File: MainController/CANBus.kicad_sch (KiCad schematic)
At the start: 1 part, among them J2 Conn_01x04_Pin

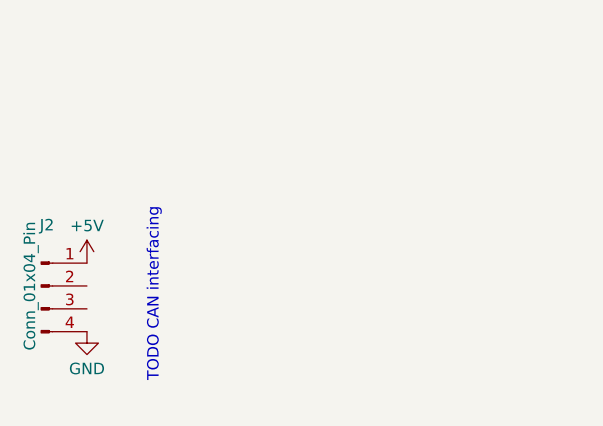
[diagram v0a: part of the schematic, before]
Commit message: WIP - Starting Voltage Measurement
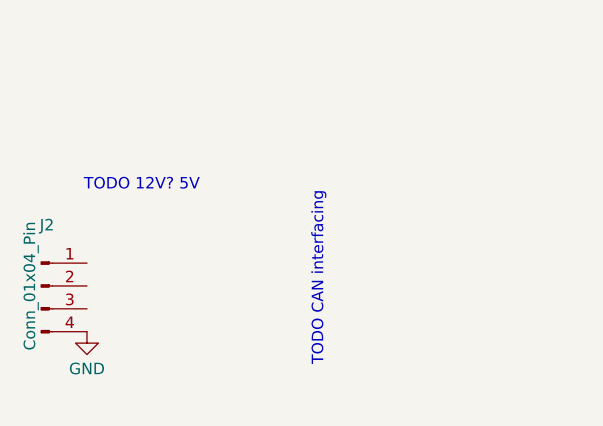
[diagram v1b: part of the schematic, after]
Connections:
- net +5V: no longer names the net of J2.1 (Pin_1)
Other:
- note added: "TODO 12V? 5V"
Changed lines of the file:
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@@
 	(text "TODO CAN interfacing"
 		(exclude_from_sim no)
-		(at 79.756 101.346 90)
+		(at 98.044 99.568 90)
+		(effects
+			(font
+				(size 1.27 1.27)
+			)
+		)
+	)
+	(text "TODO 12V? 5V"
+		(exclude_from_sim no)
+		(at 78.486 89.154 0)
 		(effects
 			(font
@@
 	(label "CAN_L"
 		(at 275.59 19.05 180)
-		(fields_autoplaced yes)
 		(effects
 			(font
@@
 	(label "CAN_H"
 		(at 275.59 15.24 180)
-		(fields_autoplaced yes)
 		(effects
 			(font
@@
 		(shape input)
 		(at 275.59 15.24 0)
-		(fields_autoplaced yes)
 		(effects
 			(font
@@
 		(shape input)
 		(at 275.59 19.05 0)
-		(fields_autoplaced yes)
 		(effects
 			(font
@@
 					(unit 1)
 				)
-			)
-		)
-	)
-	(symbol
-		(lib_id "power:+5V")
-		(at 72.39 97.79 0)
-		(unit 1)
-		(exclude_from_sim no)
-		(in_bom yes)
-		(on_board yes)
-		(dnp no)
-		(fields_autoplaced yes)
-		(property "Reference" "#PWR04"
-			(at 72.39 101.6 0)
-			(effects
-				(font
-					(size 1.27 1.27)
-				)
-				(hide yes)
-			)
-		)
-		(property "Value" "+5V"
-			(at 72.39 93.6569 0)
-			(effects
-				(font
-					(size 1.27 1.27)
-				)
-			)
-		)
-		(property "Footprint" ""
-			(at 72.39 97.79 0)
-			(effects
-				(font
-					(size 1.27 1.27)
-				)
-				(hide yes)
-			)
-		)
-		(property "Datasheet" ""
-			(at 72.39 97.79 0)
-			(effects
-				(font
-					(size 1.27 1.27)
-				)
-				(hide yes)
-			)
-		)
-		(property "Description" "Power symbol creates a global label with name \"+5V\""
-			(at 72.39 97.79 0)
-			(effects
-				(font
-					(size 1.27 1.27)
-				)
-				(hide yes)
-			)
-		)
-		(pin "1"
-		)
-		(instances
-			(project ""
-				(path "/e87d5277-7d46-4d0d-9217-730b2b1f3b51/36459019-b0f5-4788-9899-072982c72177"
-					(reference "#PWR04")
-					(unit 1)
-				)
